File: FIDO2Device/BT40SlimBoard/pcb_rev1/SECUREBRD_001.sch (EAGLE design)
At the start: 1 part, among them U1 BT40

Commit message: 回路図を更新
・周辺部品／回路を追記
・ユーザーボタン２点／USB-Cプラグメス／簡易乾電池ホルダーを実装予定
・一部の使用部品は仮の仕様（定数）です。
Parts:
- added BAT1: BAT-HLD-012-SMT, Connectors:BAT-HLD-012-SMT
- added C10, C11: 1uF, Parts:CAP_0603
- added C3, C4: 4.7uF, Parts:CAP_0603
- added C5: 0.01uF, Parts:CAP_0402K
- added C6: 10uF, Parts:CAP_0603
- added C7, C8: 0.1uF, Parts:CAP_0402K
- added CN1: TE-1734028, Connectors:TE-1734028
- added CN2: IF_4PIN, Connectors:IF_4PIN
- added CN5: IF_2PIN_SOL, Connectors:IF_2PIN_SOL
- added D1: PRTR5V0U2X, Parts:PRTR5V0U2X
- added D2, D3: PMEG2005AEA,115, Parts:PMEG2005AEA,115
- added FB1, FB2, FB3: BLM15AG121SN1D, Parts:BLM15AG121SN1D
- added LD1: APTD1608LSECK/J4-PF, Parts:APTD1608LSECK/J4-PF
- added LD2: APHD1608LSURCK, Parts:APHD1608LSURCK
- added LD3: APTD1608LZGCK, Parts:APTD1608LZGCK
- added LD4: APTD1608LVBC/D, Parts:APTD1608LVBC/D
- added R3, R6: 1.2k, Parts:RESISTOR_0402
- added R4: 1k, Parts:RESISTOR_0402
- added R5: 390, Parts:RESISTOR_0402
- added SW3: SKTADAE010, Parts:SKTADAE010
- added SW4, SW5: SKRPACE010, Parts:SKRPACE010
- added U2: XC6206P332MR-G, Parts:XC6206P332MR-G
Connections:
- new net 0V: BAT1.-, C10.2, C11.2, C3.2, C4.2, C5.2, C6.2, C7.2, C8.2, CN2.1, D1.GND, FB2.2, FB3.2, SW3.S, SW3.S1, SW4.S, SW4.S1, SW5.S, SW5.S1, U1.GND0, U1.GND1, U1.GND2, U1.GND3, U1.GND5, U1.GND6, U1.GND7, U1.GND8, U1.GND9, U2.VSS
- new net D_N: CN1.D-, D1.I/O_1, U1.DN
- new net D_P: CN1.D+, D1.I/O_2, U1.DP
- new net LED1: R6.1, U1.P0.28
- new net LED2: R3.1, U1.P0.29
- new net LED3: R4.1, U1.P0.30
- new net LED4: R5.1, U1.P0.31
- new net N$1: LD4.C, R5.2
- new net N$2: CN1.GND, FB2.1
- new net N$3: CN1.FG1, CN1.FG2, FB3.1
- new net N$4: C11.1, D2.A, U2.VOUT
- new net N$5: BAT1.+, D3.A
- new net N$6: LD3.C, R4.2
- new net N$7: LD2.C, R3.2
- new net N$8: LD1.C, R6.2
- new net P0.25: CN5.2
- new net P1.02: CN5.1
- new net RESET: SW3.P, SW3.P1, U1.RESET
- new net SW1: SW4.P, SW4.P1, U1.P0.23
- new net SW2: SW5.P, SW5.P1, U1.P0.24
- new net SWCLK: CN2.4, U1.SWCLK
- new net SWDIO: CN2.3, U1.SWDIO
- new net VBUS: C5.1, C6.1, C8.1, CN1.VBUS, D1.VCC, FB1.1
- new net VBUS_NRF: C10.1, C4.1, C7.1, FB1.2, U1.VBUS, U2.VIN
- new net VDD_NRF: C3.1, CN2.2, D2.C, D3.C, LD1.A, LD2.A, LD3.A, LD4.A, U1.VDDH, U1.VDD_NRF
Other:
- note added: "LED部"
- note added: "LED（緑色）"
- note added: "LED（赤色）"
- note added: "LED（青色）"
- note added: "LED（黄色）"
- note added: "MAIN SW"
- note added: "SUB SW"
- note added: "USBプラグ部"
- note added: "USBポートに装着時は、VBUSの5.0V-->3.3Vに降圧して供給します。 乾電池ホルダーにボタン乾電池を装着した場合は、3.0Vを供給します。"
- note added: "nRF52840アプリケーションを 書込する際に使用します。"
- note added: "バイパスコンデンサー"
- note added: "プログラミングI/F部"
- note added: "ボタン乾電池ケースは 基板の背面に実装"
- note added: "モジュール部"
- note added: "リセット回路"
- note added: "電源供給部"

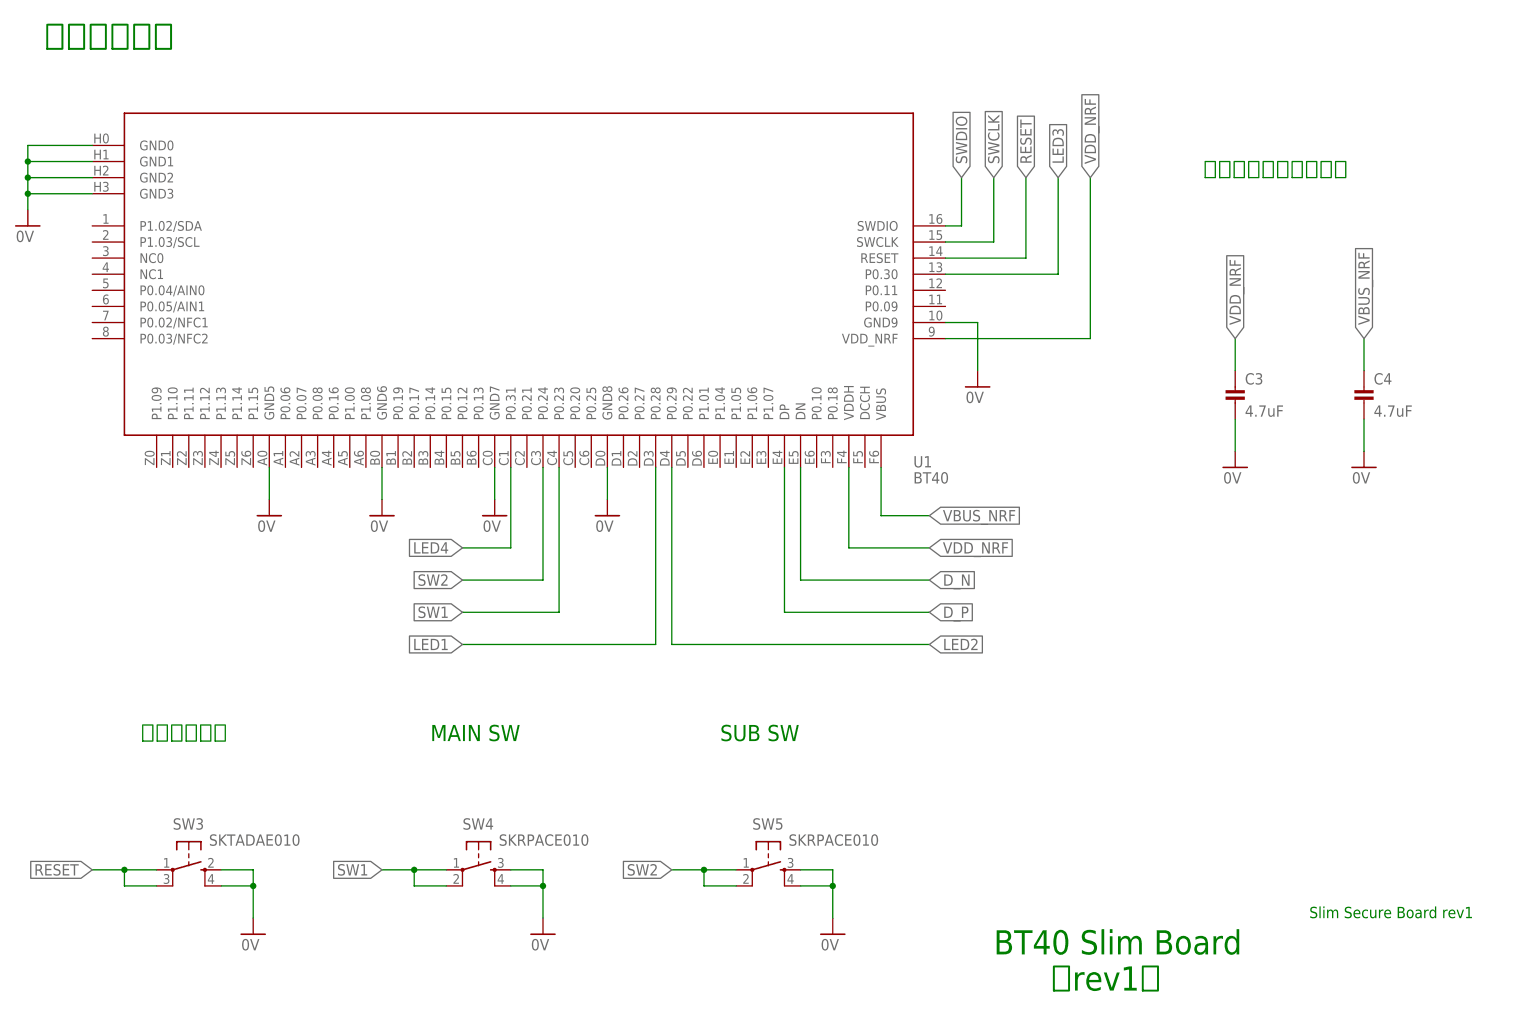
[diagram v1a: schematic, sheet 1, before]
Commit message: 回路図を更新
・ユーティリティーI/F部を追加／配線
・回路図上のコメントを修正
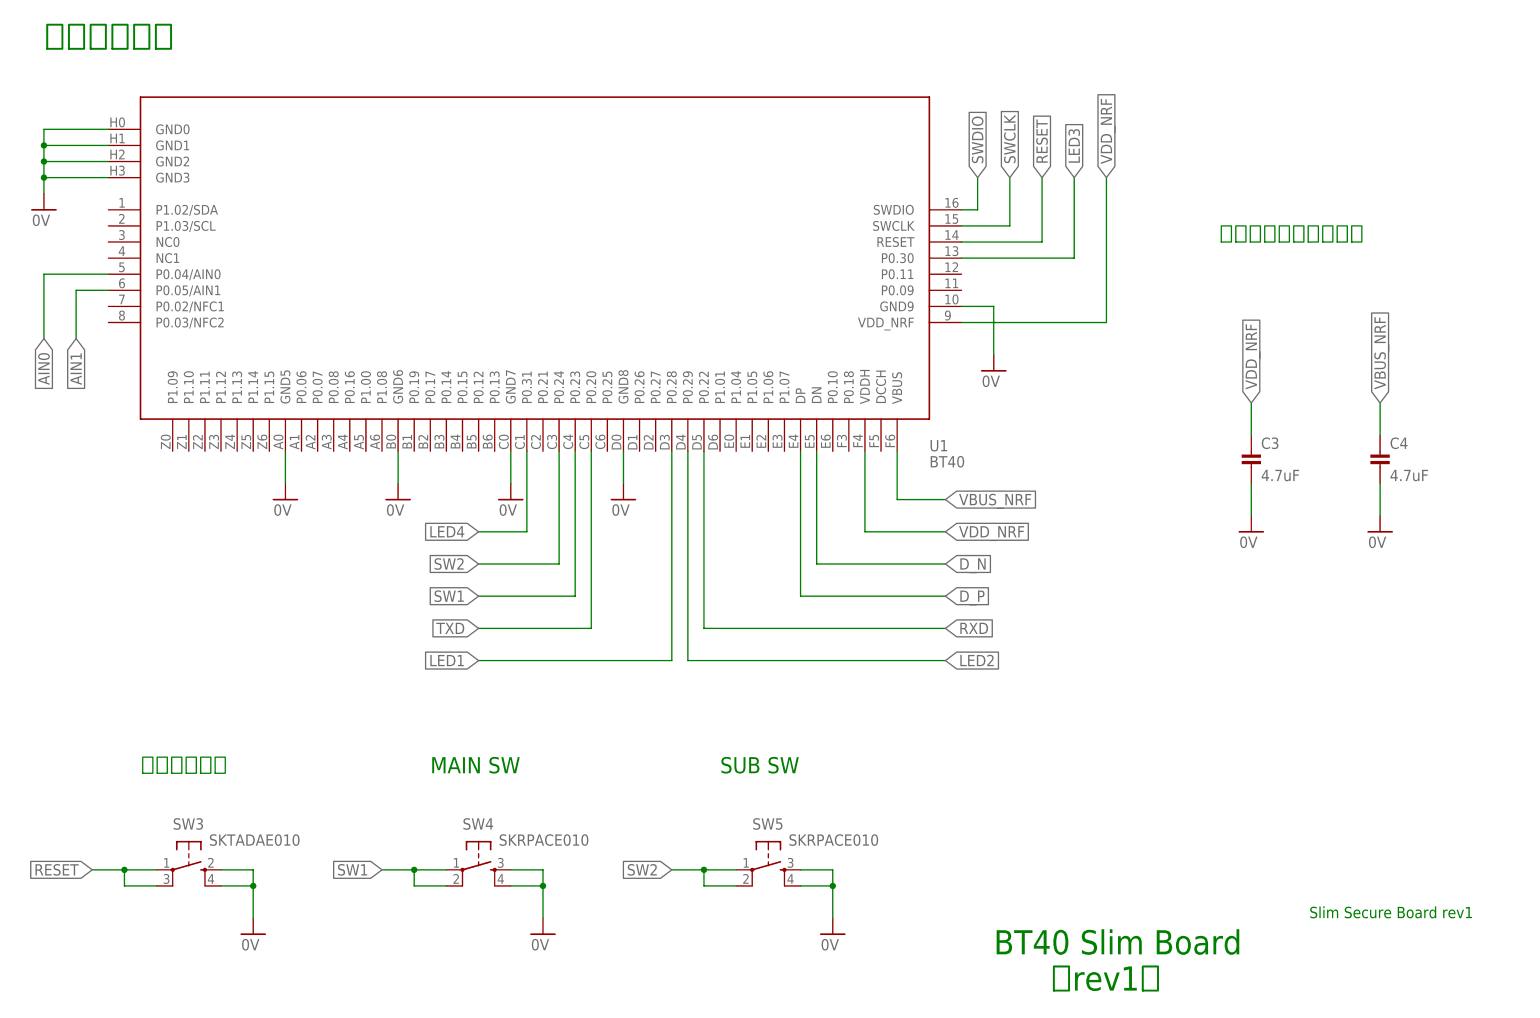
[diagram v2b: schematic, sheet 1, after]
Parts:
- removed CN5: IF_2PIN_SOL, Connectors:IF_2PIN_SOL
- added CN4: IF_3PIN_SOL, Connectors:IF_3PIN_SOL
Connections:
- removed net P0.25: CN5.2
- removed net P1.02: CN5.1
- new net AIN0: CN4.2, U1.P0.04/AIN0
- new net AIN1: CN4.3, U1.P0.05/AIN1
- new net RXD: U1.P0.22
- new net TXD: CN4.1, U1.P0.20
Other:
- note added: "TXD: UARTデバッグ出力 AIN0: 基準電圧測定入力 AIN1: 電池電圧測定入力"
- note added: "USB-Cメス プラグを実装"
- note added: "nRF5340アプリケーションを 書込する際に使用します。"
- note added: "ボタン乾電池ケースは 基板の表面に実装"
- note added: "ユーティリティーI/F部"
- note removed: "nRF52840アプリケーションを 書込する際に使用します。"
- note removed: "ボタン乾電池ケースは 基板の背面に実装"
- moved on the sheet: BAT1, C10, C11, C3, C4, D2, D3, U1, U2

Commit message: 回路図を更新
・USB-Cメスプラグを「Molex 2137160001」に差し替え
（部品入手性を考慮した措置）
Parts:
- added R2: 5.1k, Parts:RESISTOR_0402
- CN1: value TE-1734028 -> 2137160001; device Connectors:TE-1734028 -> Connectors:2137160001
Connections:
- removed net N$3: CN1.FG1, CN1.FG2, FB3.1
- removed net RXD: U1.P0.22
- new net FG: CN1.FG1, CN1.FG2, CN1.FG3, CN1.FG4, FB3.1
- new net USB_GND: CN1.GND1_A, CN1.GND1_B, CN1.GND2_A, CN1.GND2_B, FB2.1, R2.1
- net D_N: now also CN1.D_N1, CN1.D_N2; no longer CN1.D-
- net D_P: now also CN1.D_P1, CN1.D_P2; no longer CN1.D+
- net N$2: now also CN1.CC1, R2.2; no longer CN1.GND, FB2.1
- net VBUS: now also CN1.VBUS1_A, CN1.VBUS1_B, CN1.VBUS2_A, CN1.VBUS2_B; no longer CN1.VBUS
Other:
- moved on the sheet: C5, C6, C7, C8, CN2, D1, FB1, FB2, FB3, LD1, LD2, LD3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
